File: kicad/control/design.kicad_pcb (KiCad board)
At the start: 2 copper layers, 49.5 x 49.5 mm, 20 parts, among them CON1 USB-MINI-B, IC1 ATMEGA1284P-P, P1 CONN_LH, P2 CONN_RH, P3 CONN_LT, P4 CONN_RT, P5 CONN_1, P6 CONN_1, SW1 RESET, X1 12 MHz

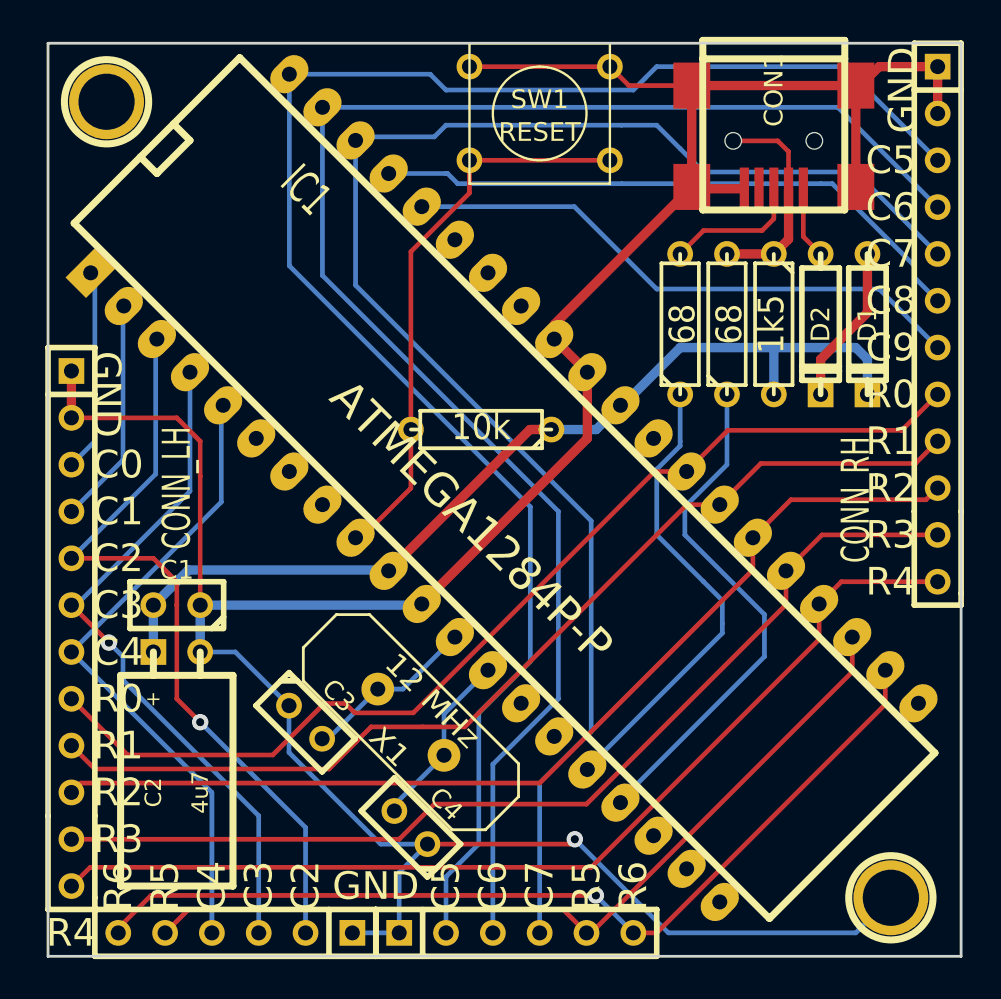
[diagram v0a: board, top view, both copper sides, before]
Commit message: converting control to a Teensy
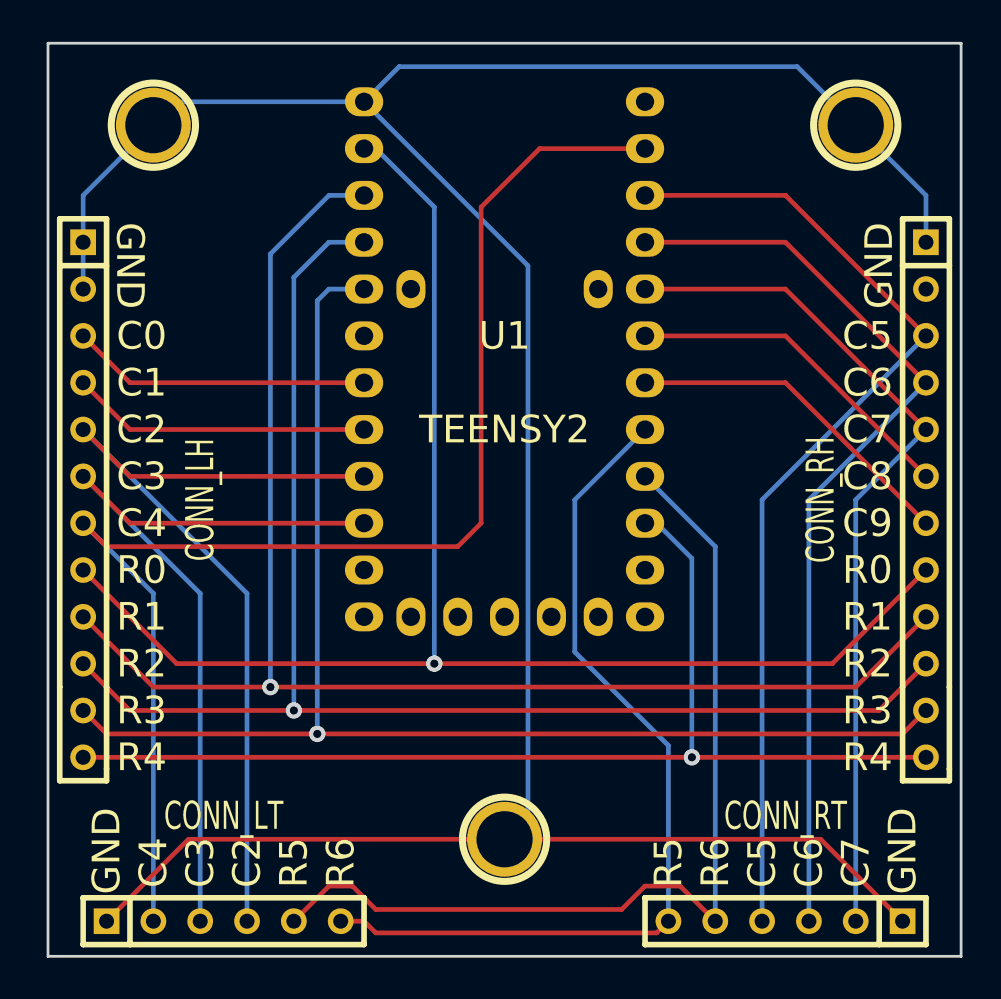
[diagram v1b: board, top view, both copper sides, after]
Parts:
- removed C1: 100nF, C1
- removed C2: 4u7, C1V5H
- removed C3, C4: 20p, C1
- removed CON1: USB-MINI-B, USB_MINI_B
- removed D1, D2: DIODE, D3
- removed IC1: ATMEGA1284P-P, DIP-40__600_ELL
- removed R1: 10k, R3
- removed R2, R3: 68, R3
- removed R4: 1k5, R3
- removed SW1: RESET, SW_PUSH_SMALL
- removed X1: 12 MHz, HC-18UV
- added P7: CONN_1, conn:1pin, F.Cu at (18.4, 17.1)
- added U1: TEENSY2, pjrc:Teensy2, F.Cu at (37.5, 28.6)
- P1, P2: footprint SIL-12 -> conn:SIL-12
- P3, P4: footprint SIL-6 -> conn:SIL-6
- P5, P6: footprint 1pin -> conn:1pin
- moved P5 45.5 mm to (37.5, 55.9)
- moved P6 42.0 mm to (56.5, 17.1)
- moved P4 14.6 mm to (52.7, 60.3), turned to 180 degrees
- moved P2 9.55 mm to (60.3, 37.5)
- moved P1 7.01 mm to (14.6, 37.5)
- moved P3 0.90 mm to (22.2, 60.3), turned to 0 degrees
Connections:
- P3 pad 2: C2 -> C4
- P3 pad 4: C4 -> C2
- P4 pad 2: C5 -> C7
- P4 pad 4: C7 -> C5
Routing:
- net VCC: track 51.8 -> 0.00 mm
- net C5: track 92.0 -> 53.8 mm
- net C4: track 35.2 -> 73.2 mm
- net C7: track 84.3 -> 46.6 mm
- net C6: track 87.2 -> 50.2 mm
- net N-0000041: track 30.8 -> 0.00 mm, vias 1 -> 0
- net N-0000038: track 28.1 -> 0.00 mm
- net N-0000019: track 25.4 -> 0.00 mm
- net R1: track 54.9 -> 78.8 mm, vias 0 -> 1
- net R0: track 56.8 -> 79.8 mm, vias 0 -> 1
- net R2: track 54.8 -> 75.9 mm, vias 0 -> 1
- net R3: track 54.9 -> 73.1 mm, vias 0 -> 1
- net C8: track 33.0 -> 18.4 mm
- net C9: track 31.2 -> 18.4 mm
- net N-0000021: track 11.7 -> 0.00 mm
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
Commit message: generated output for seeedstudio order
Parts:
- added D1: LED, led:LED-5MM, F.Cu at (24.1, 50.2)
- added D2: LED, led:LED-5MM, F.Cu at (37.5, 50.2)
- added D3: LED, led:LED-5MM, F.Cu at (50.2, 50.2)
- added R1: 500, discrete:R3, F.Cu at (19.7, 25.4)
- added R2: 500, discrete:R3, F.Cu at (22.2, 25.4)
- added R3: 500, discrete:R3, F.Cu at (24.8, 25.4)
- moved P5 0.63 mm to (37.5, 56.5)
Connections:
- net Net-(U1-Pad14) renamed L3
- U1 pad 11: Net-(U1-Pad11) -> L0
- U1 pad 12: Net-(U1-Pad12) -> L1
- U1 pad 13: Net-(U1-Pad13) -> L2
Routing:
- net Net-(D3-Pad2): track 0.00 -> 65.2 mm, vias 0 -> 1
- net Net-(D2-Pad2): track 0.00 -> 38.9 mm, vias 0 -> 1
- net Net-(D1-Pad2): track 0.00 -> 23.3 mm
- net L0: track 0.00 -> 16.8 mm, vias 0 -> 1
- net GND: track 150.2 -> 163.2 mm
- net L2: track 0.00 -> 12.0 mm, vias 0 -> 1
- net L1: track 0.00 -> 10.1 mm
- net R3: track 73.1 -> 80.9 mm
- net R4: track 59.8 -> 65.5 mm
- net R5: track 51.2 -> 55.0 mm
- net C4: track 73.2 -> 75.8 mm, vias 0 -> 2
- net R1: track 78.8 -> 79.8 mm
- net C0: track 16.3 -> 17.3 mm
- net R6: track 48.7 -> 47.8 mm, vias 0 -> 1
- net R2: track 75.9 -> 76.7 mm
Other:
- board text added: "Warren Janssens"
